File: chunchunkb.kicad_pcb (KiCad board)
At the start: 2 copper layers, 139.6 x 119.1 mm, 125 parts, among them J1 BATT, J2 OLED, SW1 SW_Push, SW10 SW_Push, SW11 SW_Push, SW12 SW_Push, SW13 SW_Push, SW14 SW_Push, SW15 SW_Push, SW16 SW_Push, SW17 SW_Push, SW18 SW_Push, SW19 SW_Push, SW2 SW_Push, SW20 SW_Push, SW21 SW_Push, SW22 SW_Push, SW23 SW_Push, SW24 SW_Push, SW25 SW_Push, SW26 SW_Push, SW27 SW_Push, SW28 SW_Push, SW29 SW_Push, SW3 SW_Push, SW30 SW_Push, SW31 EC11, SW32 SW_Push, SW33 SW_Push, SW34 SW_Push, SW35 SW_Push, SW36 SW_Push, SW4 SW_Push, SW5 SW_Push, SW6 SW_Push, SW7 SW_Push, SW8 SW_Push, SW9 SW_Push

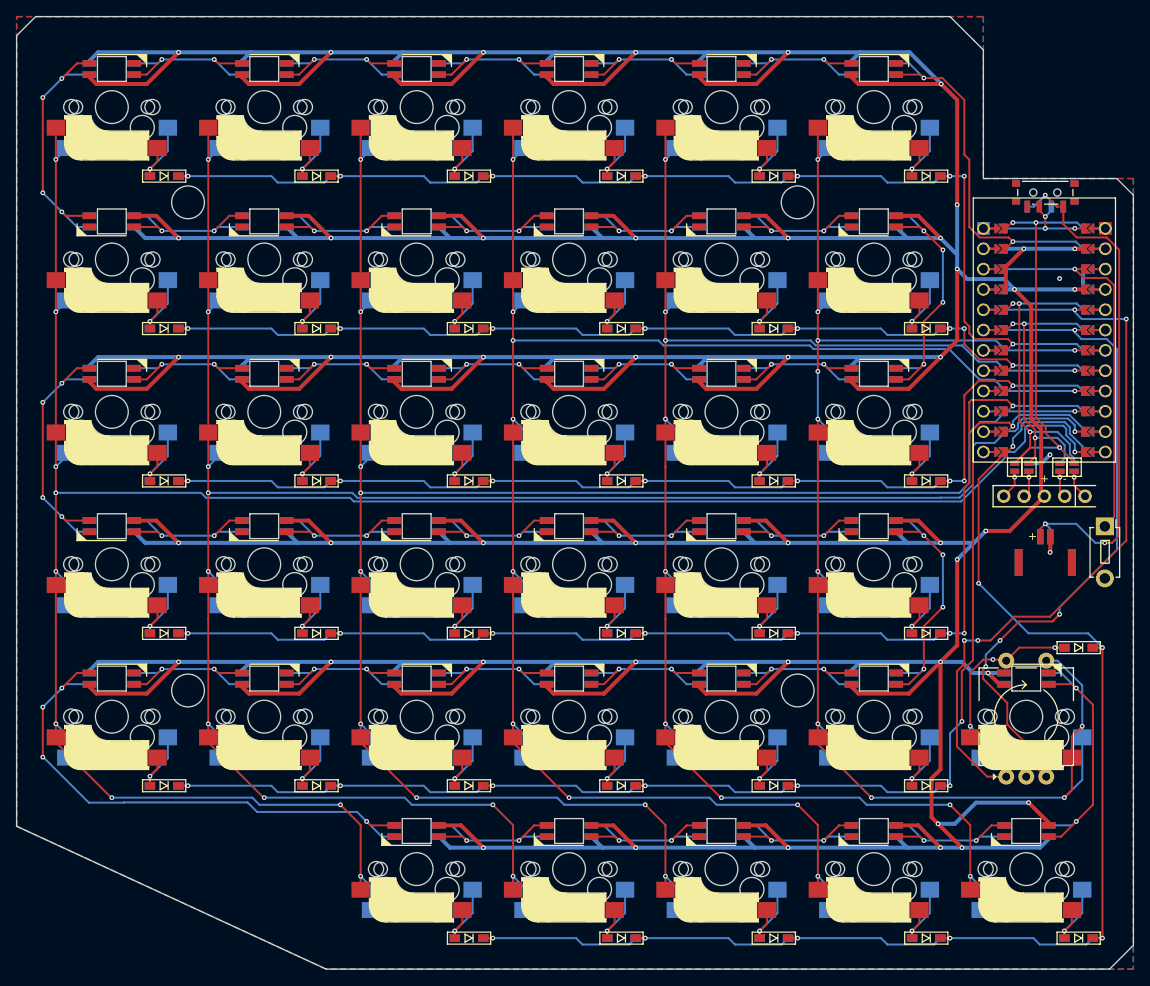
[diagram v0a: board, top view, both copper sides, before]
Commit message: chore: update pcb routing
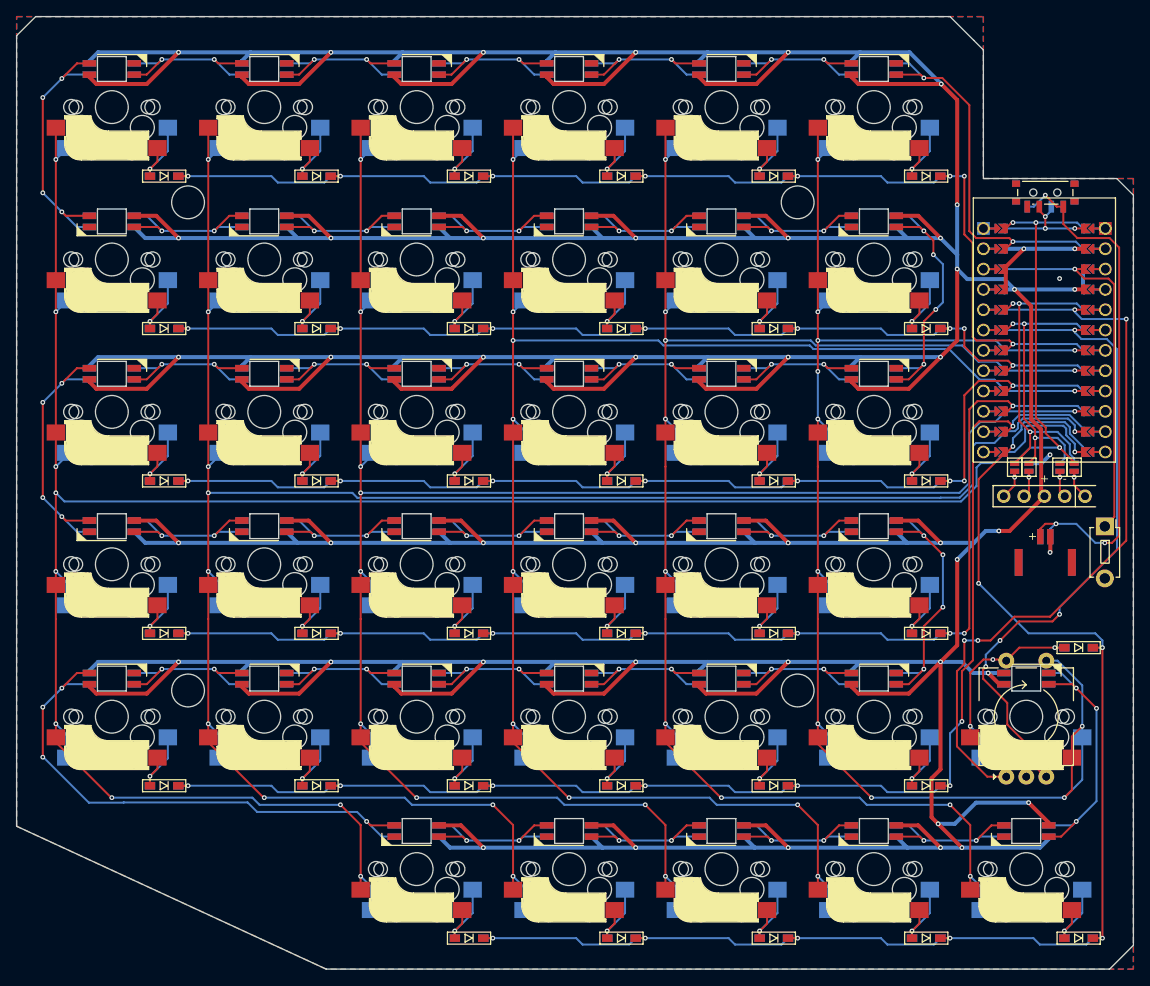
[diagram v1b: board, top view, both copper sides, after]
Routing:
- net COL 5: track 284.3 -> 285.3 mm
- net ROW 3: track 154.1 -> 153.4 mm
- net ROW 5: track 176.0 -> 176.5 mm
- net Net-(LED35-DOUT): track 34.2 -> 34.5 mm, vias 2 -> 3
